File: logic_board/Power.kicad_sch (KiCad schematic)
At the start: 14 parts, among them J3 USB_C_Receptacle_USB2.0_16P, J5 Conn_01x02, SW5 SW_SPDT, U3 MCP73832-2-OT, U4 AP2112K-3.3, U5 USBLC6-2SC6

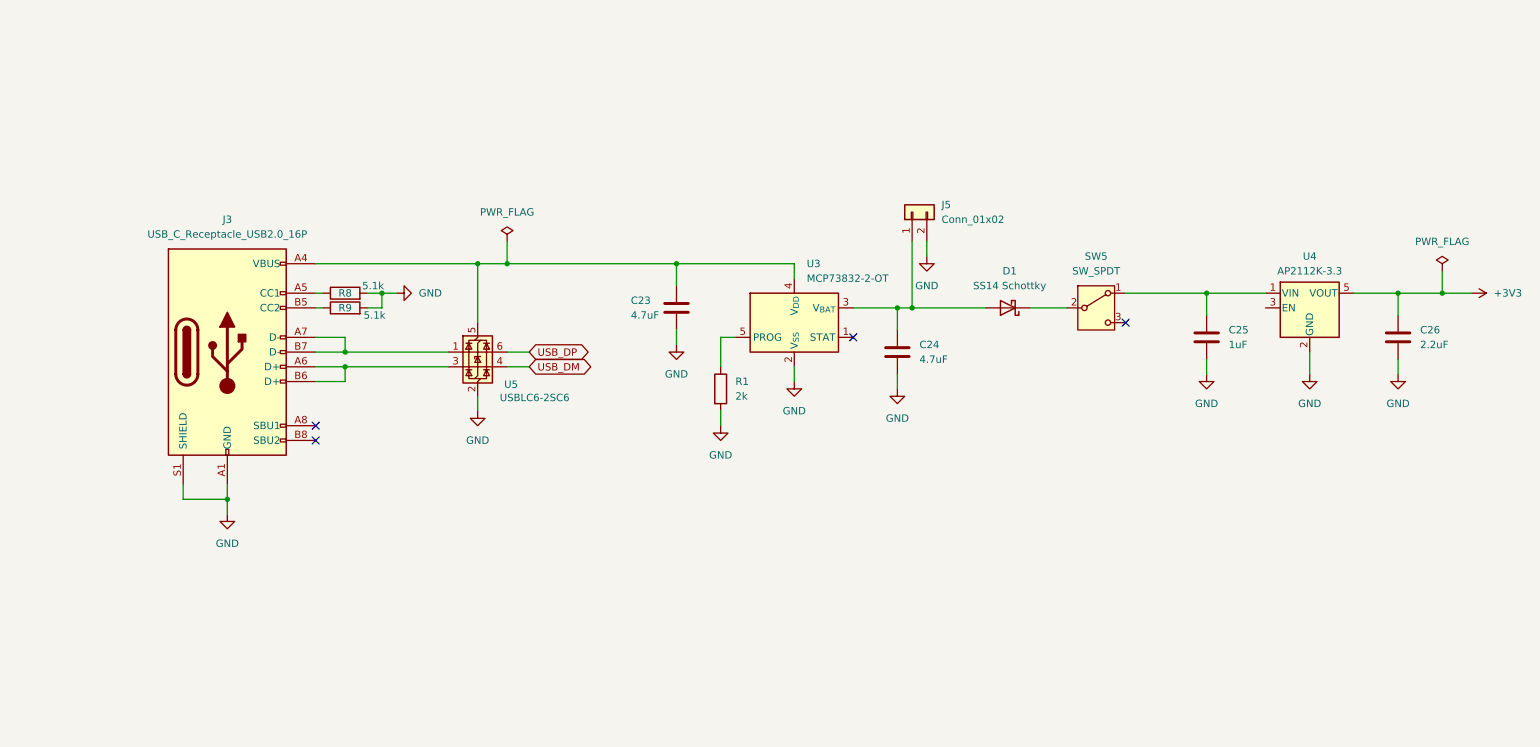
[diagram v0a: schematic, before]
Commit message: Layout power supply section
I swapped the regulator and debug connector to group the power supply components together.
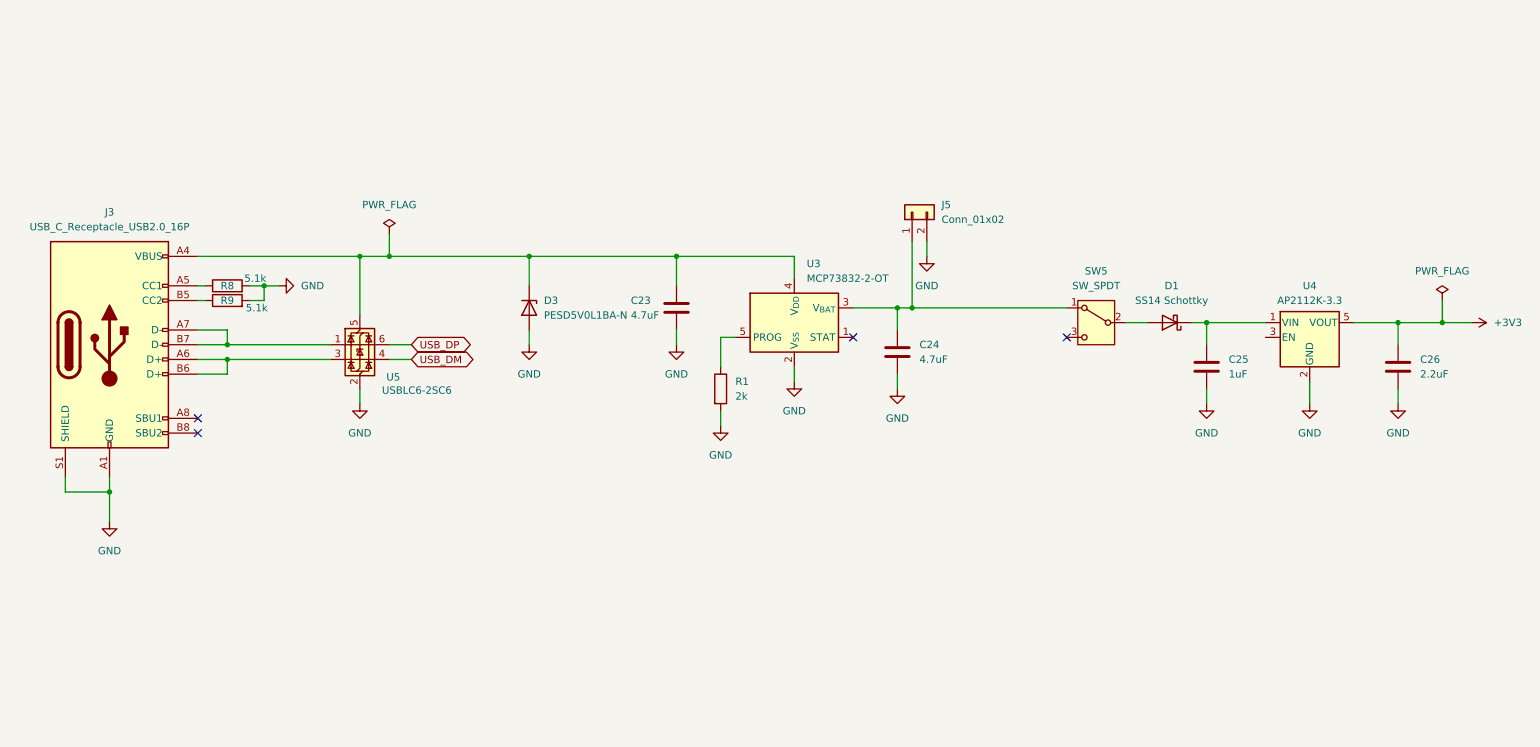
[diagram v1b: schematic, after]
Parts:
- added D3: PESD5V0L1BA-N, Diode_SMD:D_SOD-323F, symbol Diode:PESD5V0L1UL
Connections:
- net GND: now also D3.2 (A)
- net at C24.1, J5.1 (Pin_1), U3.3 (V_{BAT}): now also SW5.1 (A); no longer D1.2 (A)
- net at C23.1, J3.A4 (VBUS), J3.A9 (VBUS)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: now also D3.1 (K)
- net at C25.1, U4.1 (VIN): now also D1.1 (K); no longer SW5.1 (A)
- net at SW5.2 (B): now also D1.2 (A); no longer D1.1 (K)
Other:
- moved on the sheet: C25, C26, D1, J3, R8, R9, SW5, U4, U5

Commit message: Fix DRC and ERC violations
Also updated some design rules to be consistent with fab.
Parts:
- D3: footprint Diode_SMD:D_SOD-323F -> Diode_SMD:D_SOD-882
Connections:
- net GND: now also SW5.3 (C)
- net at C25.1, D1.1 (K), U4.1 (VIN): now also U4.3 (EN)
- no-connect marks 4 -> 3
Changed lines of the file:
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@@
 	)
 	(junction
-		(at 261.62 80.01)
+		(at 227.33 80.01)
 		(diameter 0)
 		(color 0 0 0 0)
@@
 	)
 	(junction
+		(at 224.79 80.01)
+		(diameter 0)
+		(color 0 0 0 0)
+	)
+	(junction
 		(at 167.64 77.47)
 		(diameter 0)
@@
 		(at 160.02 82.55)
 	)
-	(no_connect
-		(at 196.85 82.55)
-	)
-	(wire
-		(pts
-			(xy 220.98 80.01) (xy 231.14 80.01)
+	(wire
+		(pts
+			(xy 220.98 80.01) (xy 224.79 80.01)
 		)
 		(stroke
@@
 	(wire
 		(pts
+			(xy 224.79 76.2) (xy 224.79 80.01)
+		)
+		(stroke
+			(width 0)
+			(type default)
+		)
+	)
+	(wire
+		(pts
 			(xy 129.54 81.28) (xy 129.54 83.82)
 		)
@@
 	(wire
 		(pts
+			(xy 31.75 109.22) (xy 38.1 109.22)
+		)
+		(stroke
+			(width 0)
+			(type default)
+		)
+	)
+	(wire
+		(pts
 			(xy 149.86 87.63) (xy 149.86 90.17)
 		)
@@
 	(wire
 		(pts
+			(xy 38.1 109.22) (xy 38.1 107.95)
+		)
+		(stroke
+			(width 0)
+			(type default)
+		)
+	)
+	(wire
+		(pts
 			(xy 137.16 95.25) (xy 137.16 97.79)
 		)
@@
 	(wire
 		(pts
-			(xy 261.62 80.01) (xy 266.7 80.01)
+			(xy 193.04 82.55) (xy 196.85 82.55)
 		)
 		(stroke
@@
 	(wire
 		(pts
+			(xy 227.33 80.01) (xy 227.33 82.55)
+		)
+		(stroke
+			(width 0)
+			(type default)
+		)
+	)
+	(wire
+		(pts
 			(xy 52.07 88.9) (xy 52.07 86.36)
 		)
@@
 	(wire
 		(pts
+			(xy 231.14 82.55) (xy 227.33 82.55)
+		)
+		(stroke
+			(width 0)
+			(type default)
+		)
+	)
+	(wire
+		(pts
 			(xy 160.02 77.47) (xy 167.64 77.47)
 		)
@@
 	(wire
 		(pts
+			(xy 227.33 80.01) (xy 231.14 80.01)
+		)
+		(stroke
+			(width 0)
+			(type default)
+		)
+	)
+	(wire
+		(pts
 			(xy 129.54 68.58) (xy 129.54 73.66)
 		)
@@
 	(wire
 		(pts
-			(xy 261.62 76.2) (xy 261.62 80.01)
-		)
-		(stroke
-			(width 0)
-			(type default)
-		)
-	)
-	(wire
-		(pts
 			(xy 104.14 68.58) (xy 129.54 68.58)
 		)
@@
 	(wire
 		(pts
+			(xy 224.79 80.01) (xy 227.33 80.01)
+		)
+		(stroke
+			(width 0)
+			(type default)
+		)
+	)
+	(wire
+		(pts
 			(xy 31.75 106.68) (xy 31.75 109.22)
 		)
@@
 	(wire
 		(pts
-			(xy 254 80.01) (xy 261.62 80.01)
+			(xy 254 80.01) (xy 266.7 80.01)
 		)
 		(stroke
@@
 	)
 	(symbol
+		(lib_id "power:PWR_FLAG")
+		(at 224.79 76.2 0)
+		(unit 1)
+		(exclude_from_sim no)
+		(in_bom yes)
+		(on_board yes)
+		(dnp no)
+		(fields_autoplaced yes)
+		(property "Reference" "#FLG04"
+			(at 224.79 74.295 0)
+			(effects
+				(font
+					(size 1.27 1.27)
+				)
+				(hide yes)
+			)
+		)
+		(property "Value" "PWR_FLAG"
+			(at 224.79 71.12 0)
+			(effects
+				(font
+					(size 1.27 1.27)
+				)
+			)
+		)
+		(property "Footprint" ""
+			(at 224.79 76.2 0)
+			(effects
+				(font
+					(size 1.27 1.27)
+				)
+				(hide yes)
+			)
+		)
+		(property "Datasheet" "~"
+			(at 224.79 76.2 0)
+			(effects
+				(font
+					(size 1.27 1.27)
+				)
+				(hide yes)
+			)
+		)
+		(property "Description" "Special symbol for telling ERC where power comes from"
+			(at 224.79 76.2 0)
+			(effects
+				(font
+					(size 1.27 1.27)
+				)
+				(hide yes)
+			)
+		)
+		(pin "1"
+		)
+		(instances
+			(project ""
+				(path "/b7b37fe1-b409-497a-9440-d94d882f6459/78b9c77c-6b0c-47f1-b5e8-ea96354c74d6"
+					(reference "#FLG04")
+					(unit 1)
+				)
+			)
+		)
+	)
+	(symbol
 		(lib_id "Device:R")
 		(at 137.16 91.44 0)
@@
 	(symbol
 		(lib_id "power:GND")
+		(at 193.04 82.55 270)
+		(unit 1)
+		(exclude_from_sim no)
+		(in_bom yes)
+		(on_board yes)
+		(dnp no)
+		(fields_autoplaced yes)
+		(property "Reference" "#PWR057"
+			(at 186.69 82.55 0)
+			(effects
+				(font
+					(size 1.27 1.27)
+				)
+				(hide yes)
+			)
+		)
+		(property "Value" "GND"
+			(at 189.23 82.5499 90)
+			(effects
+				(font
+					(size 1.27 1.27)
+				)
+				(justify right)
+			)
+		)
+		(property "Footprint" ""
+			(at 193.04 82.55 0)
+			(effects
+				(font
+					(size 1.27 1.27)
+				)
+				(hide yes)
+			)
+		)
+		(property "Datasheet" ""
+			(at 193.04 82.55 0)
+			(effects
+				(font
+					(size 1.27 1.27)
+				)
+				(hide yes)
+			)
+		)
+		(property "Description" "Power symbol creates a global label with name \"GND\" , ground"
+			(at 193.04 82.55 0)
+			(effects
+				(font
+					(size 1.27 1.27)
+				)
+				(hide yes)
+			)
+		)
+		(pin "1"
+		)
+		(instances
+			(project ""
+				(path "/b7b37fe1-b409-497a-9440-d94d882f6459/78b9c77c-6b0c-47f1-b5e8-ea96354c74d6"
+					(reference "#PWR057")
+					(unit 1)
+				)
+			)
+		)
+	)
+	(symbol
+		(lib_id "power:GND")
 		(at 31.75 114.3 0)
 		(unit 1)
@@
 	)
 	(symbol
+		(lib_id "power:PWR_FLAG")
+		(at 38.1 107.95 0)
+		(unit 1)
+		(exclude_from_sim no)
+		(in_bom yes)
+		(on_board yes)
+		(dnp no)
+		(fields_autoplaced yes)
+		(property "Reference" "#FLG03"
+			(at 38.1 106.045 0)
+			(effects
+				(font
+					(size 1.27 1.27)
+				)
+				(hide yes)
+			)
+		)
+		(property "Value" "PWR_FLAG"
+			(at 38.1 102.87 0)
+			(effects
+				(font
+					(size 1.27 1.27)
+				)
+			)
+		)
+		(property "Footprint" ""
+			(at 38.1 107.95 0)
+			(effects
+				(font
+					(size 1.27 1.27)
+				)
+				(hide yes)
+			)
+		)
+		(property "Datasheet" "~"
+			(at 38.1 107.95 0)
+			(effects
+				(font
+					(size 1.27 1.27)
+				)
+				(hide yes)
+			)
+		)
+		(property "Description" "Special symbol for telling ERC where power comes from"
+			(at 38.1 107.95 0)
+			(effects
+				(font
+					(size 1.27 1.27)
+				)
+				(hide yes)
+			)
+		)
+		(pin "1"
+		)
+		(instances
+			(project "logic_board"
+				(path "/b7b37fe1-b409-497a-9440-d94d882f6459/78b9c77c-6b0c-47f1-b5e8-ea96354c74d6"
+					(reference "#FLG03")
+					(unit 1)
+				)
+			)
+		)
+	)
+	(symbol
 		(lib_id "power:GND")
 		(at 172.72 68.58 0)
@@
 	)
 	(symbol
-		(lib_id "power:PWR_FLAG")
-		(at 261.62 76.2 0)
-		(unit 1)
-		(exclude_from_sim no)
-		(in_bom yes)
-		(on_board yes)
-		(dnp no)
-		(fields_autoplaced yes)
-		(property "Reference" "#FLG02"
-			(at 261.62 74.295 0)
-			(effects
-				(font
-					(size 1.27 1.27)
-				)
-				(hide yes)
-			)
-		)
-		(property "Value" "PWR_FLAG"
-			(at 261.62 71.12 0)
-			(effects
-				(font
-					(size 1.27 1.27)
-				)
-			)
-		)
-		(property "Footprint" ""
-			(at 261.62 76.2 0)
-			(effects
-				(font
-					(size 1.27 1.27)
-				)
-				(hide yes)
-			)
-		)
-		(property "Datasheet" "~"
-			(at 261.62 76.2 0)
-			(effects
-				(font
-					(size 1.27 1.27)
-				)
-				(hide yes)
-			)
-		)
-		(property "Description" "Special symbol for telling ERC where power comes from"
-			(at 261.62 76.2 0)
-			(effects
-				(font
-					(size 1.27 1.27)
-				)
-				(hide yes)
-			)
-		)
-		(pin "1"
-		)
-		(instances
-			(project ""
-				(path "/b7b37fe1-b409-497a-9440-d94d882f6459/78b9c77c-6b0c-47f1-b5e8-ea96354c74d6"
-					(reference "#FLG02")
-					(unit 1)
-				)
-			)
-		)
-	)
-	(symbol
 		(lib_id "Power_Protection:USBLC6-2SC6")
 		(at 74.93 83.82 0)
@@
 			)
 		)
-		(property "Datasheet" "https://jlcpcb.com/partdetail/Korean_HropartsElec-TYPE_C_31_M12/C165948"
+		(property "Datasheet" "https://www.usb.org/sites/default/files/documents/usb_type-c.zip"
 			(at 35.56 83.82 0)
 			(effects
@@
 			)
 		)
-		(property "Description" "Right Angle Type-C SMD USB Connector"
+		(property "Description" "USB 2.0-only 16P Type-C Receptacle connector"
 			(at 31.75 83.82 0)
 			(effects
@@
 			)
 		)
-		(property "Footprint" "Diode_SMD:D_SOD-323F"
+		(property "Footprint" "Diode_SMD:D_SOD-882"
 			(at 99.06 77.47 0)
 			(effects
@@
 			)
 		)
-		(property "Datasheet" "https://jlcpcb.com/partdetail/BORN-PESD5V0L1BAN/C920305"
+		(property "Datasheet" "https://assets.nexperia.com/documents/data-sheet/PESD5V0L1UL.pdf"
 			(at 109.22 77.47 0)
 			(effects
@@
 			)
 		)
-		(property "Description" "Low capacitance unidirectional ESD protection diode, 5V, SOD-323"
+		(property "Description" "Low capacitance unidirectional ESD protection diode, 5V, SOD-882"
 			(at 111.76 77.47 0)
 			(effects

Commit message: All signals now routed.
A bit rough, needs some cleanup.
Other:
- moved on the sheet: C23, C24, C25, C26, D1, D3, J3, J5, R1, R8, R9, SW5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

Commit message: Fix some incorrect footprints/symbols
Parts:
- SW5: LCSC part number SSSS211603 -> C125040
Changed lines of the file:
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@@
 			)
 		)
-		(property "LCSC part number" "SSSS211603"
+		(property "LCSC part number" "C125040"
 			(at 201.93 92.71 0)
 			(effects

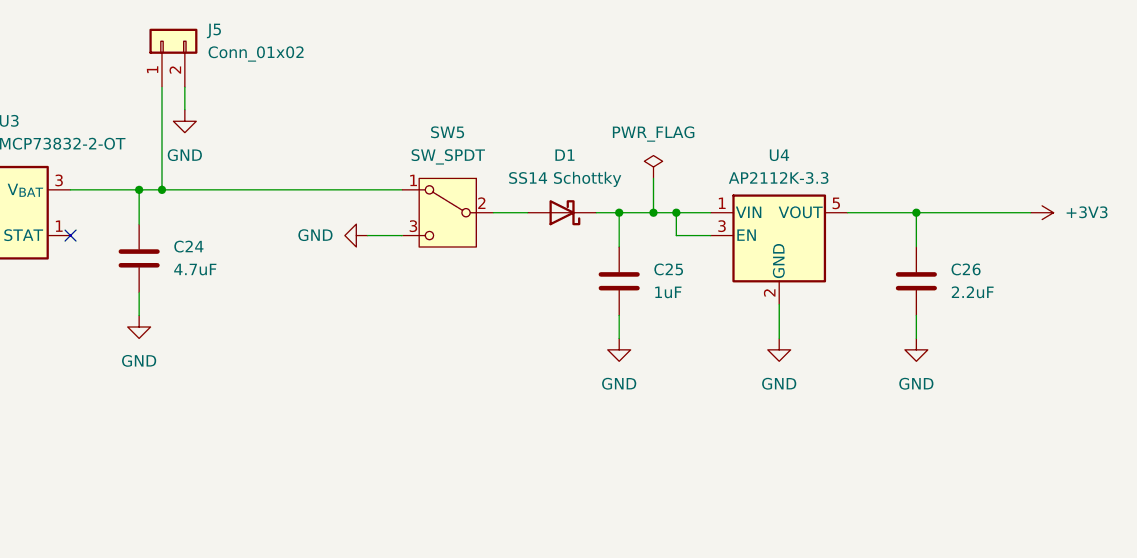
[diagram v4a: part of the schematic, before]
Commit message: Power switch connects to en pin on LDO rather than switching power directly.
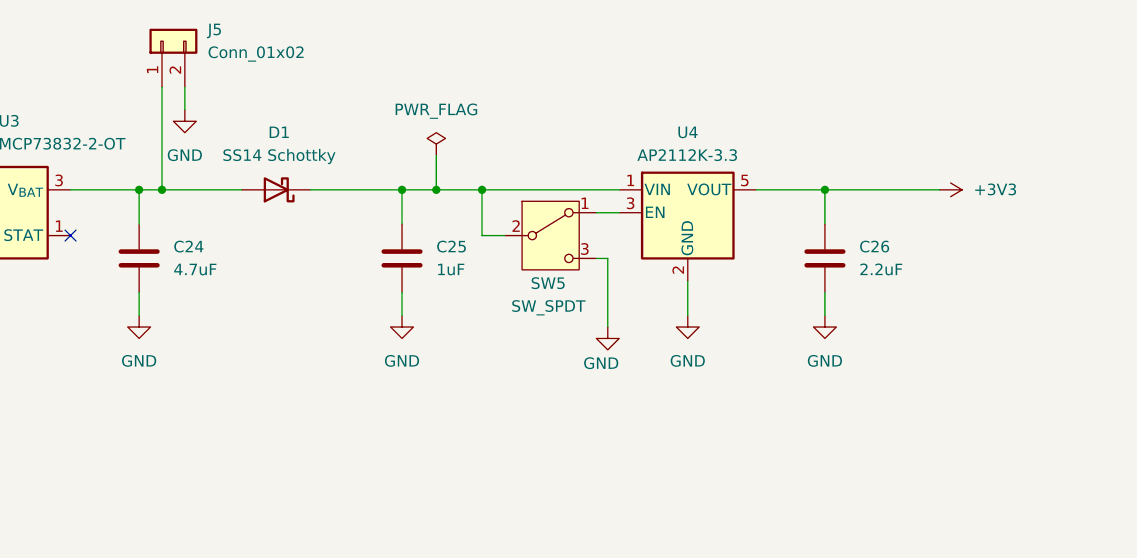
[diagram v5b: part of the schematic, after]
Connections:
- net at C24.1, J5.1 (Pin_1), U3.3 (V_{BAT}): now also D1.2 (A); no longer SW5.1 (A)
- net at C25.1, D1.1 (K), U4.1 (VIN): now also SW5.2 (B); no longer U4.3 (EN)
- new net: SW5.1 (A), U4.3 (EN)
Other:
- moved on the sheet: C25, C26, D1, SW5, U4

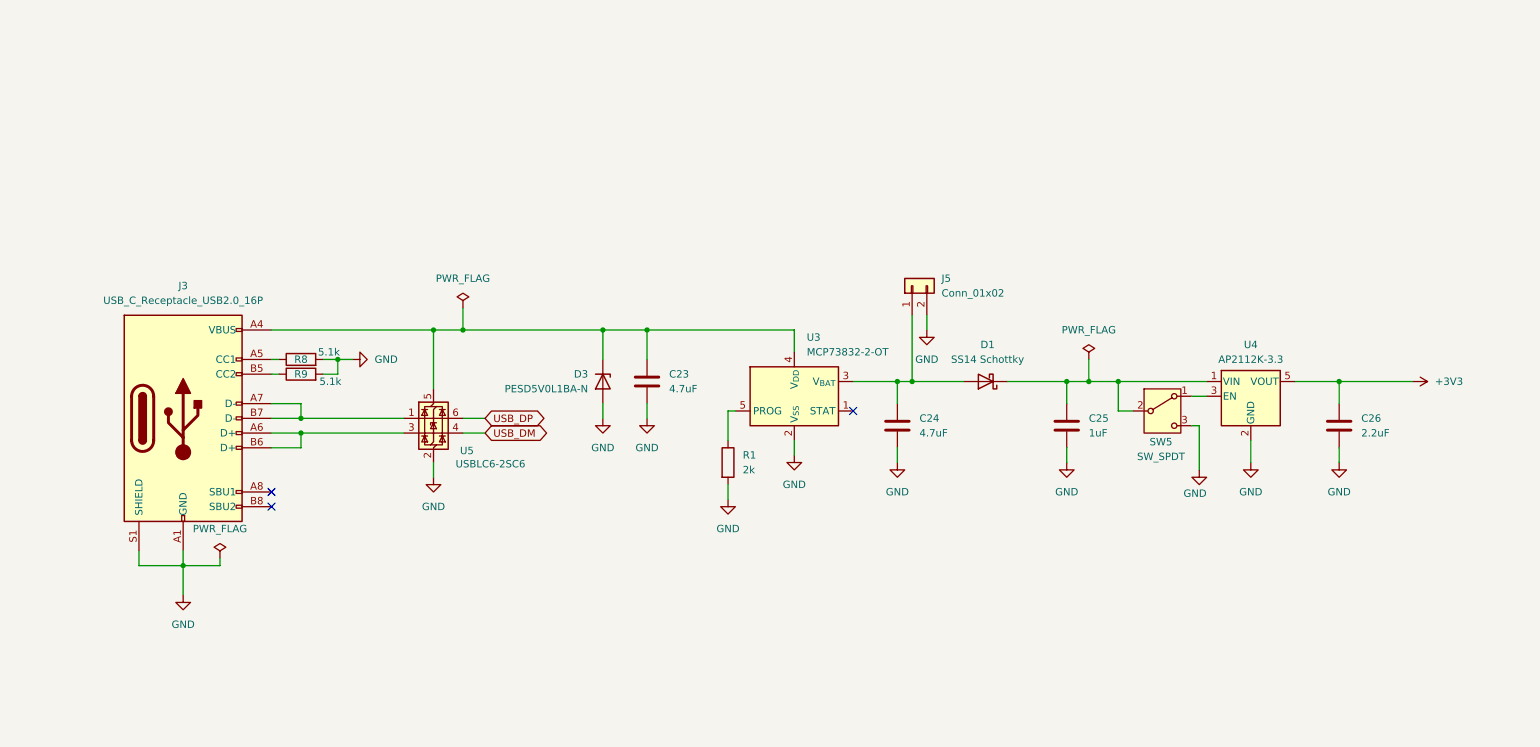
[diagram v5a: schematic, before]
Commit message: Change charger to BQ25185
This one has power steering so it can run the MCU and charge simultaneously without charge termination problems.
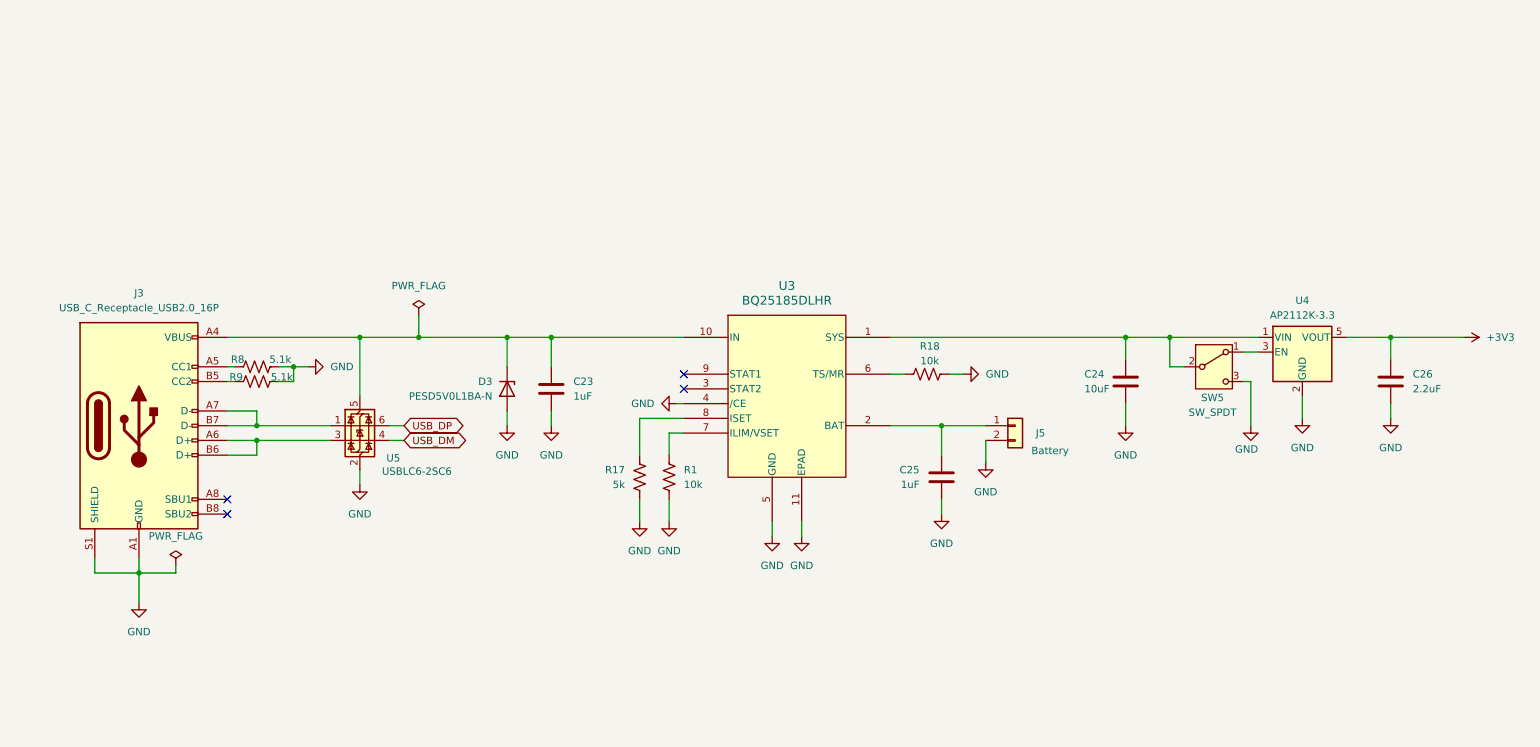
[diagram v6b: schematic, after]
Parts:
- removed D1: SS14 Schottky, Diode_SMD:D_SMA, symbol Device:D_Schottky
- removed R1: 2k, Resistor_SMD:R_0603_1608Metric, symbol Device:R
- removed U3: MCP73832-2-OT, Package_TO_SOT_SMD:SOT-23-5, symbol Battery_Management:MCP73832-2-OT
- added R1, R18: 10k, symbol Device:R_US
- added R17: 5k, Resistor_SMD:R_0603_1608Metric, symbol Device:R_US
- added U3: BQ25185DLHR, Custom_Footprints:WSON10_DLH_TEX, symbol Custom_Symbols:BQ25185DLHR
- C23: value 4.7uF -> 1uF; Type (none) -> 10V/X7R
- C24: value 4.7uF -> 10uF; footprint Capacitor_SMD:C_0603_1608Metric -> Capacitor_SMD:C_0805_2012Metric; Type (none) -> 10V/X7R
- C25: Type (none) -> 10v/X7R
- J5: value Conn_01x02 -> Battery
- R8, R9: symbol Device:R -> Device:R_US
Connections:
- net GND: now also R1.2, R17.2, R18.2, U3.11 (EPAD), U3.4 (/CE), U3.5 (GND)
- net at C24.1: now also SW5.2 (B), U4.1 (VIN), U3.1 (SYS); no longer J5.1 (Pin_1)
- net at C23.1, D3.1 (K), J3.A4 (VBUS)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: now also U3.10 (IN)
- new net: R1.1, U3.7 (ILIM/VSET)
- new net: C25.1, J5.1 (Pin_1), U3.2 (BAT)
- new net: R18.1, U3.6 (TS/MR)
- new net: R17.1, U3.8 (ISET)
- no-connect marks 3 -> 4
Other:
- moved on the sheet: C23, C24, C26, D3, J3, J5, SW5, U4, U5
